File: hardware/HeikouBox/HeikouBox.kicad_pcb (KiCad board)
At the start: 2 copper layers, 100 x 100 mm, 194 parts, among them J101 5V, J201 Conn_02x05_Odd_Even, J202 Conn_02x08_Odd_Even, J301 DB15_Female_HighDensity_Mount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, J302 AudioJack3_SwitchTR, J501 Micro_SD_Card_TFP09-2-12B, J503 PS/2, Q301 MMBT3904, Q302 MMBT3904, Q303 MMBT3904, Q304 MMBT3904, Q305 MMBT3904, Q306 MMBT3904, Q307 MMBT3904, Q502 BSS138, Q503 BSS138, SW501 Left, SW502 Right, SW503 Up, SW504 Down, U101 LD1117S33TR, U102 LD1117S25TR, U103 LD1117S12TR, U201 HeikouBox-Core, U202 74HCU04, U401 K4S281632-UC60, U501 STM32-BluePill-Socket, Y201 14.31818MHz, Y202 28.37516MHz

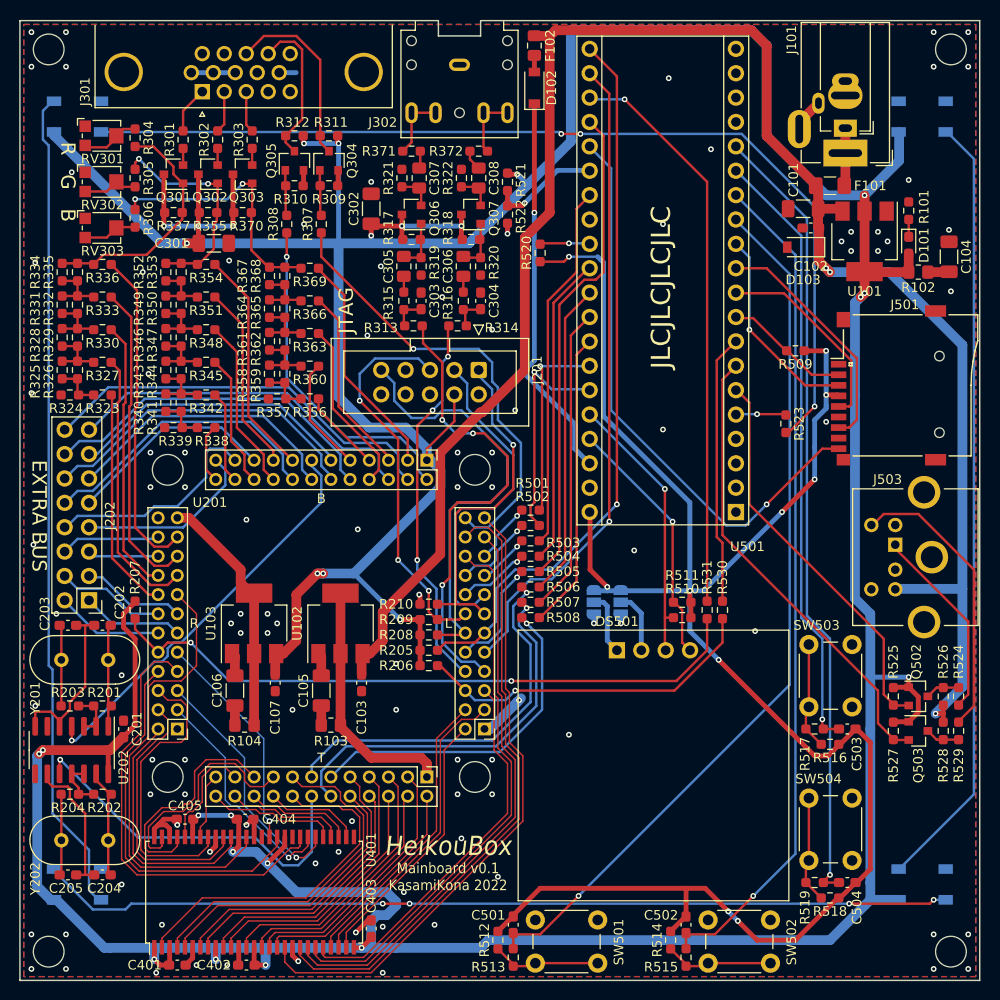
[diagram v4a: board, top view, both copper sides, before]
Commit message: Cleanup, add rounded corners, bigger diode
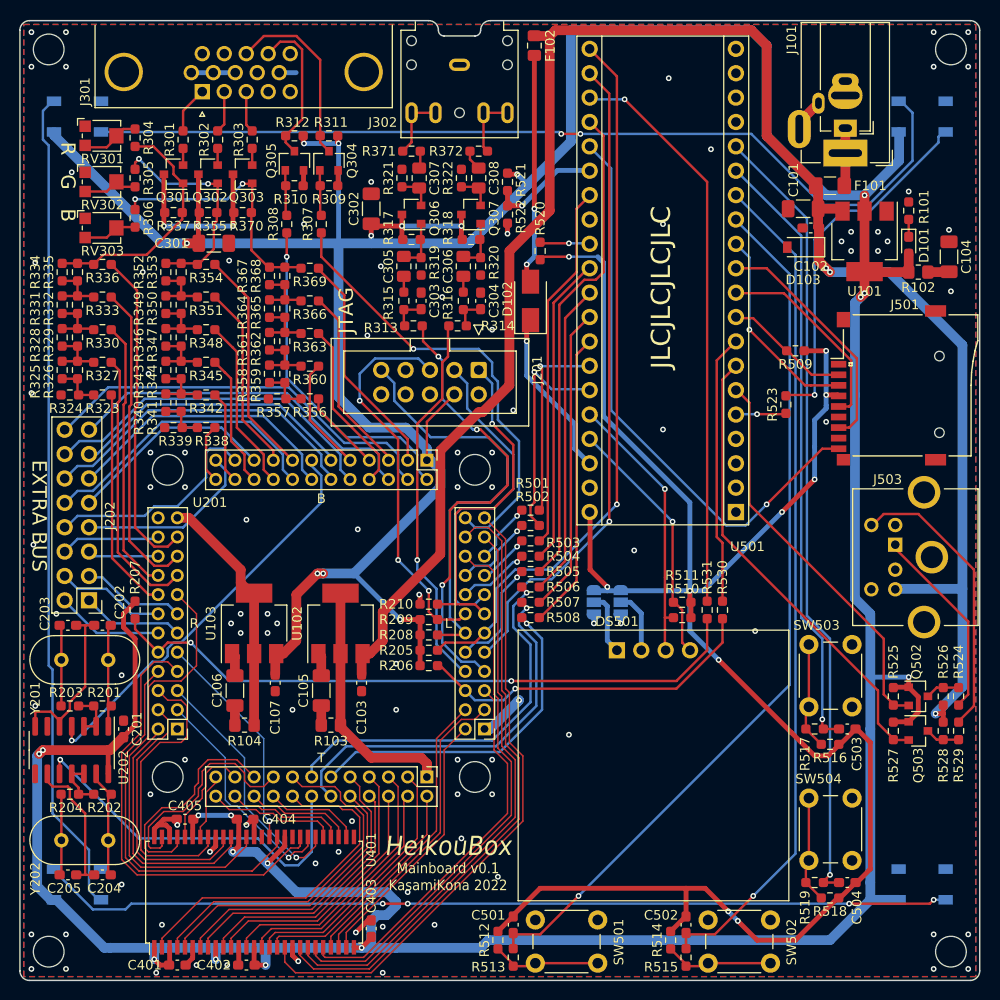
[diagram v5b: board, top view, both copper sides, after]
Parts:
- D102: value D -> M7; footprint Diode_SMD:D_SOD-123 -> Diode_SMD:D_SMA
- moved D102 22.2 mm to (68.0, 49.6)
- moved R523 2.00 mm to (94.6, 60.4), turned to 90 degrees
- moved R520 0.20 mm to (69.0, 44.4)
- renumbered D504 to D501, D501 to D502, D502 to D503, D503 to D504
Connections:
- D501 pad 2: Net-(D504-Pad2) -> Net-(D501-Pad2)
- D501 pad 4: Net-(D503-Pad2) (its old number) -> Net-(D501-Pad4)
- D502 pad 4: Net-(D501-Pad4) -> Net-(D501-Pad2)
- D504 pad 2: Net-(D503-Pad2) (its old number) -> Net-(D504-Pad2)
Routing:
- net Net-(D501-Pad2): track 0.00 -> 96.6 mm, vias 0 -> 2
- net Net-(D503-Pad2) (its old number): track 81.4 -> 0.00 mm
- net Net-(D501-Pad4): track 102.5 -> 37.9 mm, vias 3 -> 1
- net /part1-power/VUSB: track 40.5 -> 17.8 mm
- net Net-(D102-Pad2): track 1.73 -> 24.1 mm, vias 0 -> 2
- net /part3-av/LSIGMA: track 48.9 -> 47.6 mm
- net /part2-core/jtag_TDI: track 45.1 -> 44.5 mm
- net /part3-av/RSIGMA: track 39.6 -> 39.5 mm, vias 3 -> 1
- net /part1-power/GND: vias 101 -> 99
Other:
- outline, holes or cut-outs redrawn
- board text added: "2 1"
- board text added: "VCC GND"
- board text removed: "1 2"
- board text removed: "GND VCC"

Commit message: More tidy up, move vias
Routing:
- net /part2-core/mdb5: track 40.3 -> 37.7 mm
- net /part1-power/GND: track 75.9 -> 74.7 mm, vias 99 -> 90
- net /part2-core/mdb6: track 40.3 -> 39.4 mm
- net /part2-core/mdb7: track 35.4 -> 34.5 mm
- net /part2-core/xbus12: track 29.4 -> 30.0 mm
- net /part3-av/RED2: track 28.4 -> 27.9 mm

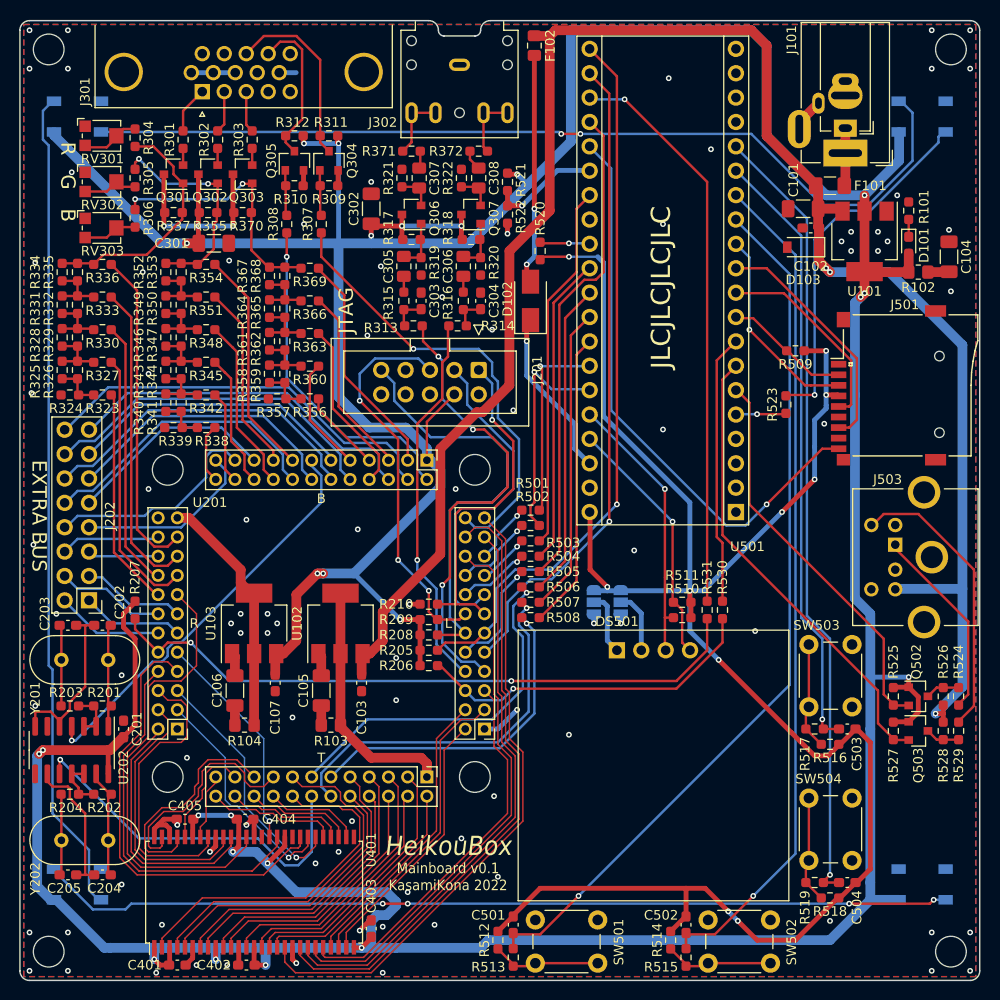
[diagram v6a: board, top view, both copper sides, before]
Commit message: Fix bluepill position, routing cleanup
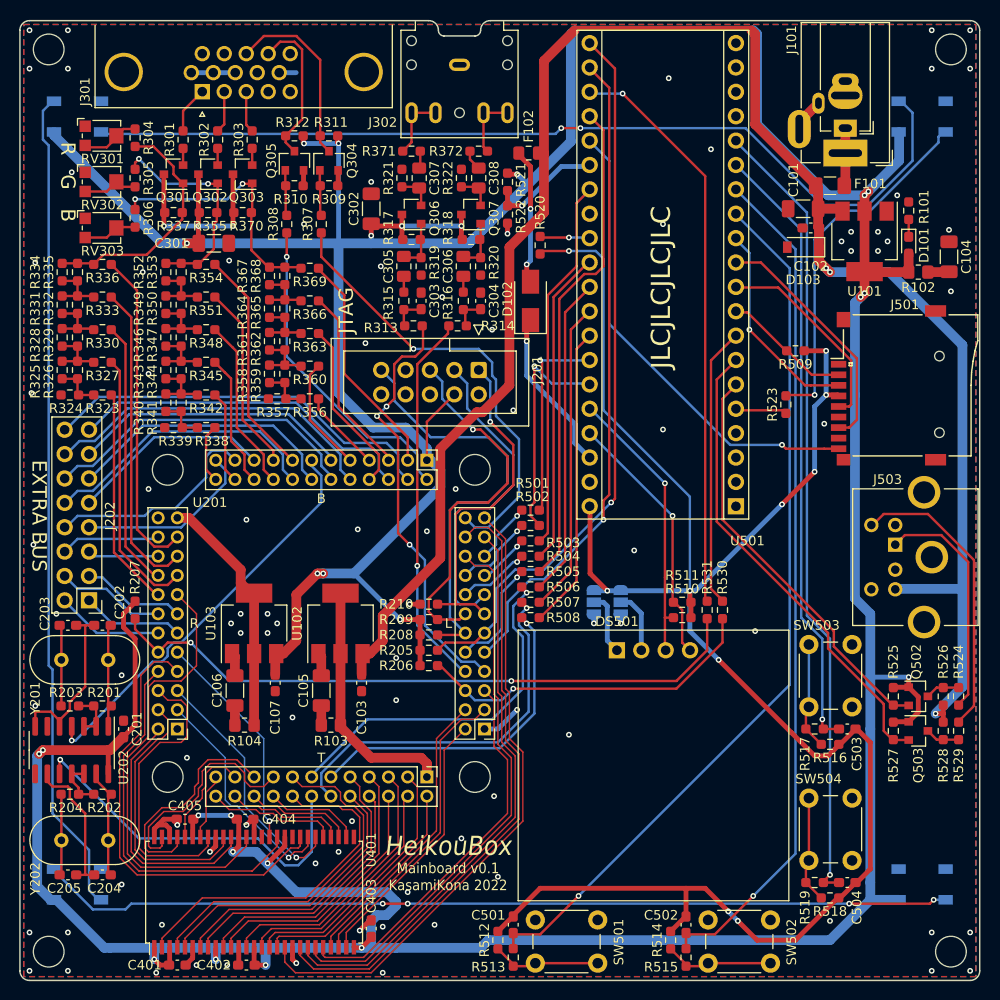
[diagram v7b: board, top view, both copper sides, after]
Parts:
- moved F102 11.2 mm to (67.8, 34.2), turned to 180 degrees
- moved R520 0.60 mm to (69.0, 43.8)
- moved U501 0.60 mm to (89.4, 71.0)
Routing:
- net /part5-hub/SD_DET: track 60.4 -> 49.2 mm
- net Net-(D102-Pad2): track 24.1 -> 14.2 mm
- net Net-(J503-Pad1): track 20.3 -> 24.5 mm
- net /part3-av/LSIGMA: track 48.0 -> 44.3 mm
- net /part1-power/5V: track 196.2 -> 194.2 mm
- net /part2-core/jtag_TMS: track 40.6 -> 38.7 mm, vias 3 -> 1
- net /part5-hub/KEYBOARD_DAT: track 41.3 -> 43.0 mm
- net /part3-av/NVSYNC: track 35.0 -> 33.7 mm
- net /part5-hub/KEYBOARD_CLK: track 48.5 -> 49.7 mm
- net /part5-hub/CFG_NSTAT_R: track 28.2 -> 29.3 mm
- net /part2-core/xbus9: track 30.7 -> 29.8 mm
- net /part2-core/xbus15: track 42.5 -> 41.7 mm
- net /part2-core/xbus13: track 36.5 -> 35.7 mm
- net /part2-core/xbus10: track 29.6 -> 28.7 mm
- net /part2-core/xbus8: track 21.9 -> 21.1 mm
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
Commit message: Cleanup, change silkscreen reference size
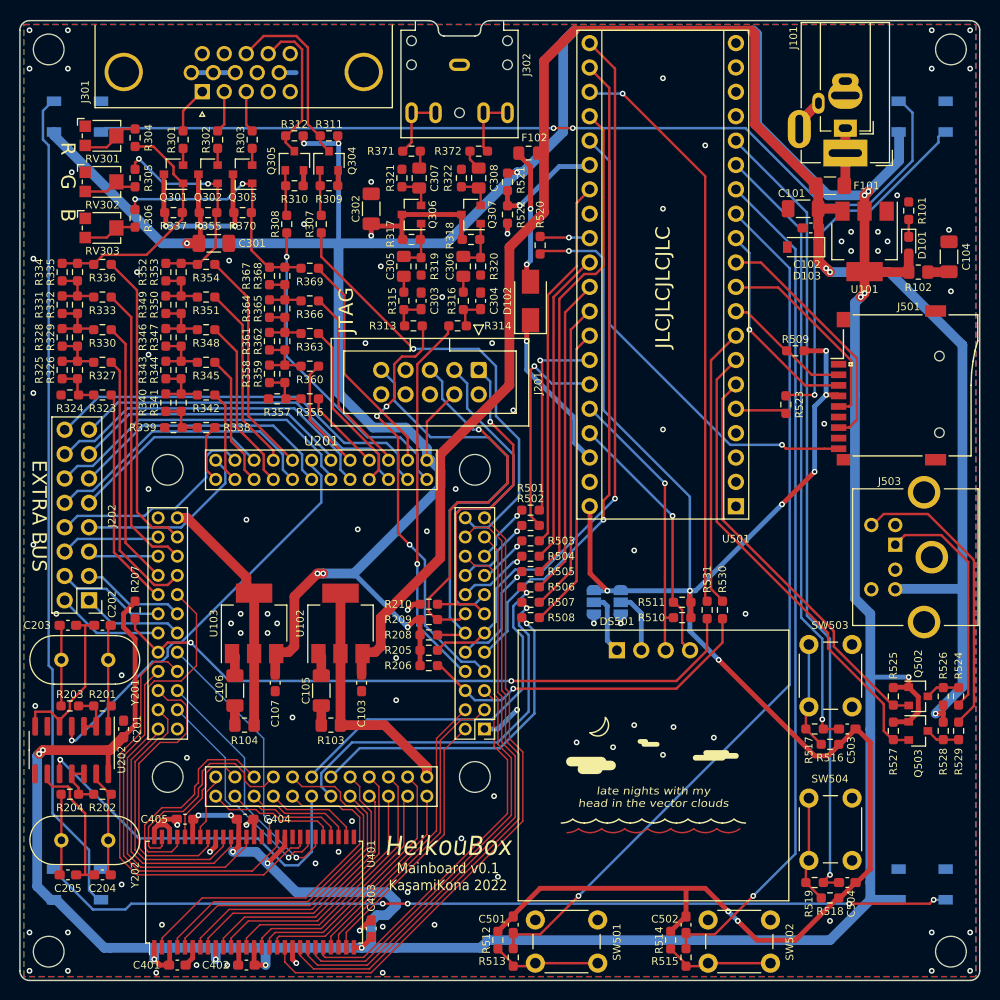
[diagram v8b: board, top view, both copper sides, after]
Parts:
- turned U201 to 0 degrees
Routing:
- net /part3-av/RED4: track 34.1 -> 32.2 mm
- net /part3-av/RED3: track 32.7 -> 30.8 mm
- net /part1-power/3V3: track 558.3 -> 556.7 mm, vias 28 -> 26
- net /part1-power/GND: track 74.7 -> 75.1 mm, vias 91 -> 96
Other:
- board text added: "late nights with my head in the vector clouds"
